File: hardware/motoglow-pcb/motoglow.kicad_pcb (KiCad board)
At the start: 2 copper layers, 80 x 60 mm, 35 parts, among them J1 12V IN, J2 RUN0 L, J3 RUN1 R, J4 RUN2 ENG, J5 RUN3 TAIL, J6 BAR, Q1 IRF4905, U1 R-78E5.0-1.0, U2 74AHCT125N, U3 Pico 2 W

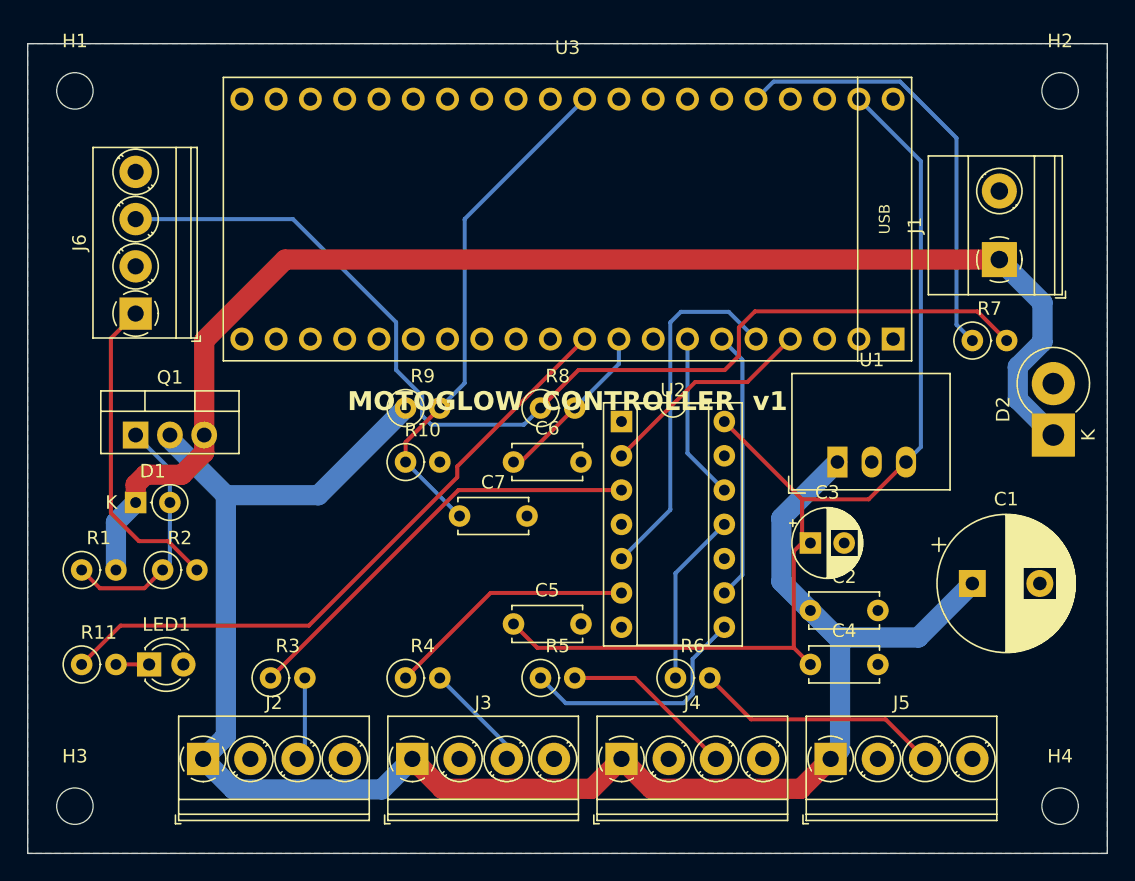
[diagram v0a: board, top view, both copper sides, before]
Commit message: Rev B: make the board and the enclosure fit each other, and prove it
Revision A had both halves verified and mutually impossible. The case was built
for a 75 x 55 mm board that had become 80 x 60, its four posts missed the real
mounting holes by 2.5 mm on each axis, and all six panel connectors' bodies
landed inside components -- 19 collisions. Nothing in the project compared the
two, so nothing complained.

mech.py now holds every number that couples them and both sides read it. The
case no longer keeps its own copy of the board size, hole positions or port
list: export_pcb_data.py writes those from the real board into pcb_data.scad,
and cad/build.sh runs the exporter and verify_fit.py before rendering, so a
board change that breaks the case stops the build instead of the print.

verify_fit.py checks the board fits, the posts land on real holes, no connector
nut or barrel intersects a component, and nothing in the keep-out band is too
tall. It has a negative test: forcing revision A's geometry back in makes it
report all 19 collisions.

Defects found by auditing what had only ever been asserted from memory:

- The status LED was wired backwards. KiCad's Device:LED pin 1 is the cathode,
  not the anode, so it could never have lit.
- The connector holes were cut 4.8 mm into a 5.2 mm wall and were blind. The
  case had two different numbers for one wall thickness.
- The stock KiCad electrolytic footprint carries no polarity mark at all, which
  PARTS.md claimed it did. Every orientation-sensitive part now has its function
  printed beside the pad, generated from the netlist: G/D/S at Q1, Vin/GND/Vout
  at U1, + at the electrolytics, K/A at the LED, pin order under each strip
  connector.

Checked against datasheets rather than memory, and all correct as built:
IRF4905 G-D-S, R-78E5.0 Vin-GND-Vout, 74AHCT125 pinout, the Pico's 17.78 mm row
pitch, and pad 1 = cathode on all three vertical diode footprints.

Added: C8, a gate-source cap giving Q1 a ~1 ms soft start inste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
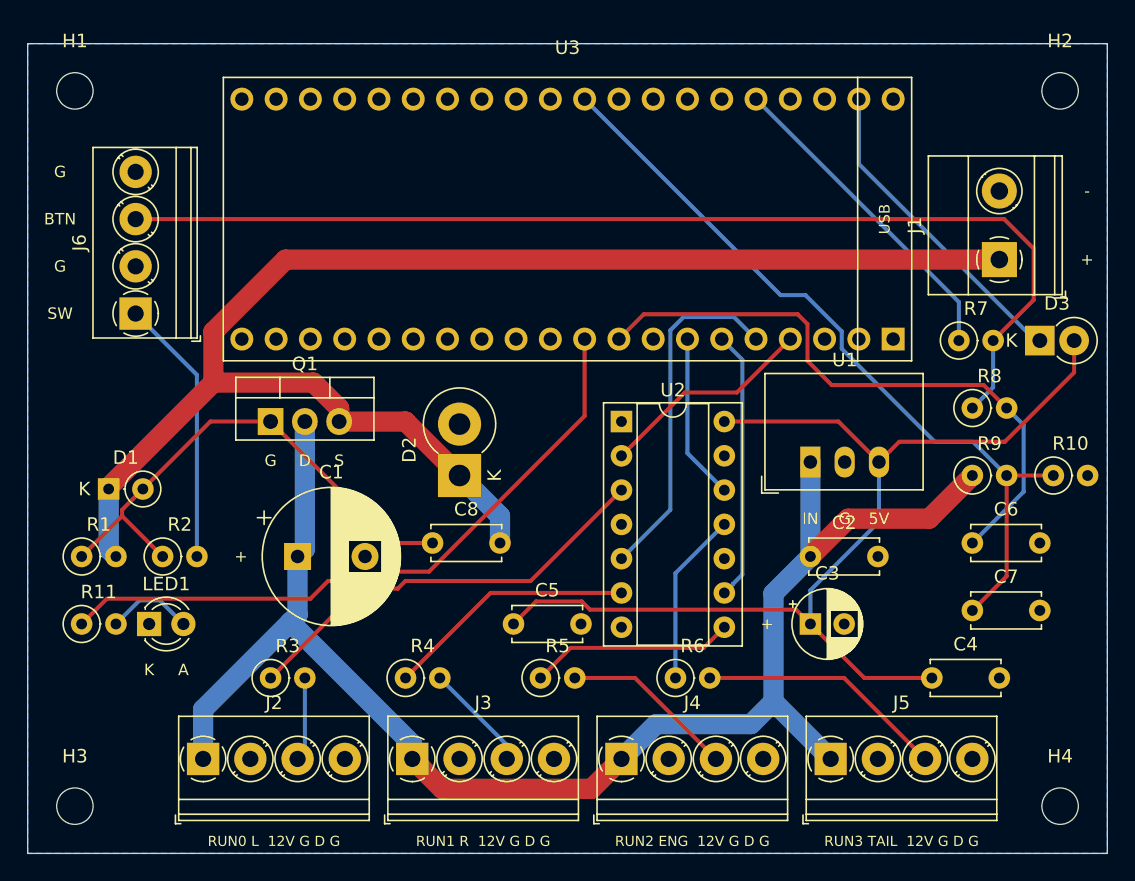
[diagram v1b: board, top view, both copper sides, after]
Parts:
- added C8: 100nF, C_Disc_D5.0mm_W2.5mm_P5.00mm, F.Cu at (30.0, 37.0)
- added D3: 1N5819, D_DO-41_SOD81_P2.54mm_Vertical_KathodeUp, F.Cu at (75.0, 22.0)
- moved C1 50.0 mm to (20.0, 38.0)
- moved R10 48.0 mm to (76.0, 32.0)
- moved D2 44.1 mm to (32.0, 32.0)
- moved R9 42.3 mm to (70.0, 32.0)
- moved C7 38.6 mm to (70.0, 42.0)
- moved C6 34.5 mm to (70.0, 37.0)
- moved R8 32.0 mm to (70.0, 27.0)
- moved Q1 10.0 mm to (18.0, 28.0)
- moved C4 9.06 mm to (67.0, 47.0)
- moved C3 6.00 mm to (58.0, 43.0)
- moved C2 4.00 mm to (58.0, 38.0)
- moved LED1 3.00 mm to (9.00, 43.0)
- moved R11 3.00 mm to (4.00, 43.0)
- moved D1 2.24 mm to (6.00, 33.0)
- moved U1 2.00 mm to (58.0, 31.0)
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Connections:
- LED1 pad 1: LED_A -> GND
- LED1 pad 2: GND -> LED_A
- U3 pad 39: +5V -> VSYS
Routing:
- net GP6: track 12.7 -> 46.1 mm
- net VSYS: track 0.00 -> 23.6 mm
- net +12VSW: track 131.8 -> 111.7 mm
- net VSENSE: track 38.0 -> 58.1 mm
- net GATE: track 18.4 -> 38.4 mm
- net BAT+: track 98.9 -> 108.5 mm
- net +3V3: track 32.6 -> 24.1 mm
- net LED_A: track 2.46 -> 6.45 mm
- net SW_A: track 23.7 -> 19.9 mm
- net Y3: track 18.3 -> 15.2 mm
- net BTN: track 79.4 -> 81.1 mm
- net GP7: track 47.7 -> 49.4 mm
- net +5V: track 81.4 -> 80.4 mm
- net GP3: track 26.5 -> 25.9 mm
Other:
- board text added: "+"
- board text added: "-"
- board text added: "5V"
- board text added: "A"
- board text added: "BTN"
- board text added: "D"
- board text added: "D1 BZX55C15 D2 1.5KE18A D3 1N5819 pin1 = K"
- board text added: "G"
- board text added: "IN"
- board text added: "K"
- board text added: "LED1 pin1 = K, pin2 = A"
- board text added: "MOTOGLOW CONTROLLER v1.1"
- board text added: "RUN0 L 12V G D G"
- board text added: "RUN1 R 12V G D G"
- board text added: "RUN2 ENG 12V G D G"
- board text added: "RUN3 TAIL 12V G D G"
- board text added: "S"
- board text added: "SW"
- board text removed: "D1 BZX55C15 D2 1.5KE18A pin 1 = cathode"
- board text removed: "MOTOGLOW CONTROLLER v1"
